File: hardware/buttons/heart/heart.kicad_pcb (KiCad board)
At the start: 2 copper layers, 24.5 x 26.3 mm, 10 parts, among them J1 Conn_01x03, J2 Conn_01x03

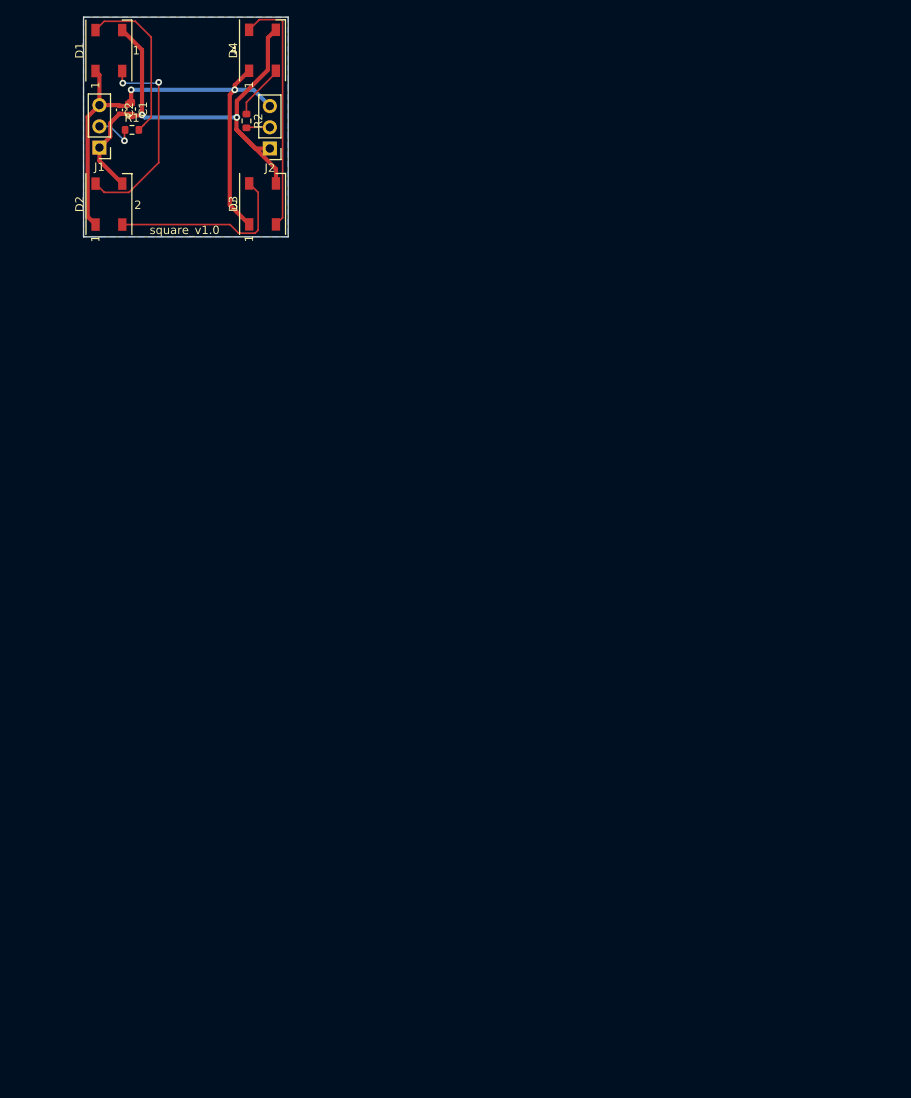
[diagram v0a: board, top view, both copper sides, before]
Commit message: Add heart button
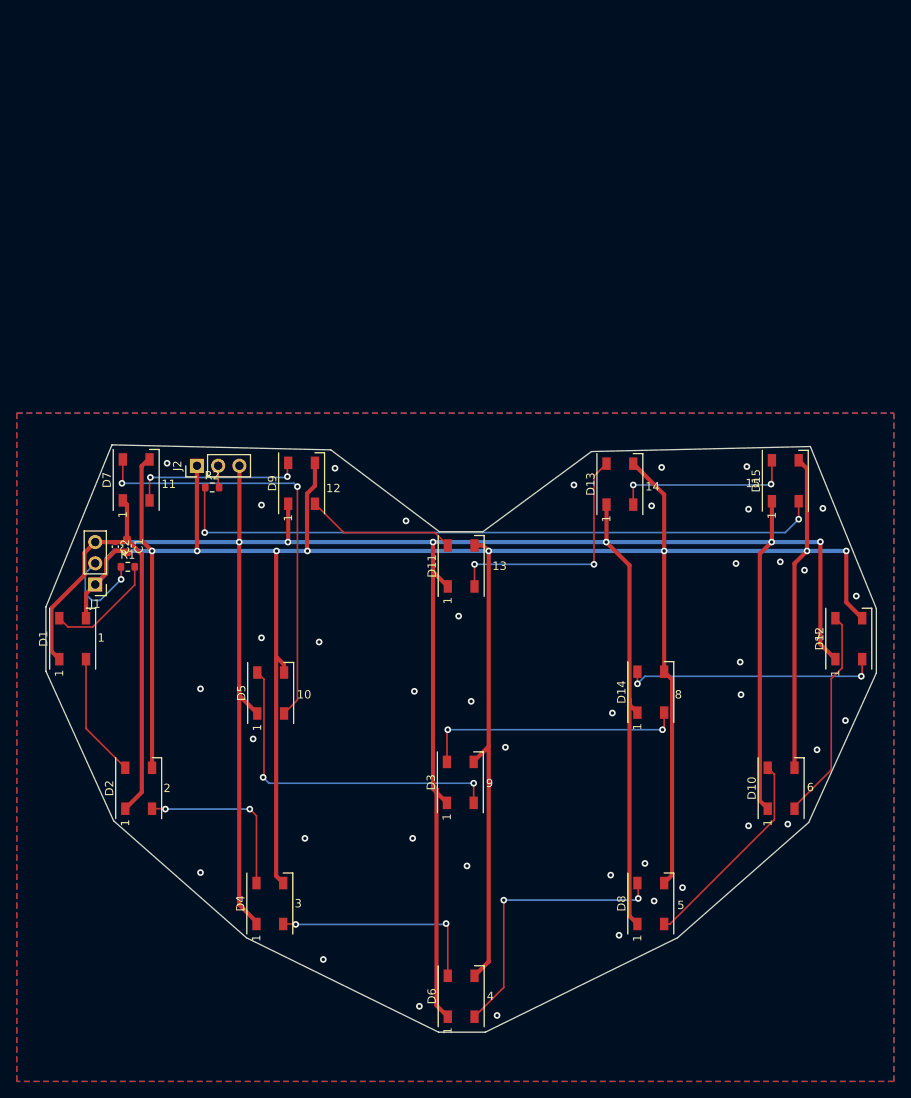
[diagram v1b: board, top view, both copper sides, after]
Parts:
- added D10: WS2812B, LED_SMD:LED_WS2812B_PLCC4_5.0x5.0mm_P3.2mm, F.Cu at (121.5, 124.9)
- added D11: WS2812B, LED_SMD:LED_WS2812B_PLCC4_5.0x5.0mm_P3.2mm, F.Cu at (83.2, 98.3)
- added D12: WS2812B, LED_SMD:LED_WS2812B_PLCC4_5.0x5.0mm_P3.2mm, F.Cu at (129.6, 107.0)
- added D13: WS2812B, LED_SMD:LED_WS2812B_PLCC4_5.0x5.0mm_P3.2mm, F.Cu at (102.2, 88.5)
- added D14: WS2812B, LED_SMD:LED_WS2812B_PLCC4_5.0x5.0mm_P3.2mm, F.Cu at (105.9, 113.4)
- added D15: WS2812B, LED_SMD:LED_WS2812B_PLCC4_5.0x5.0mm_P3.2mm, F.Cu at (122.0, 88.1)
- added D3: WS2812B, LED_SMD:LED_WS2812B_PLCC4_5.0x5.0mm_P3.2mm, F.Cu at (83.1, 124.2)
- added D5: WS2812B, LED_SMD:LED_WS2812B_PLCC4_5.0x5.0mm_P3.2mm, F.Cu at (60.4, 113.5)
- added D7: WS2812B, LED_SMD:LED_WS2812B_PLCC4_5.0x5.0mm_P3.2mm, F.Cu at (44.3, 88.0)
- added D8: WS2812B, LED_SMD:LED_WS2812B_PLCC4_5.0x5.0mm_P3.2mm, F.Cu at (105.9, 138.7)
- added D9: WS2812B, LED_SMD:LED_WS2812B_PLCC4_5.0x5.0mm_P3.2mm, F.Cu at (64.1, 88.4)
- moved D6 115.7 mm to (83.2, 149.8)
- moved D4 83.7 mm to (60.3, 138.7)
- moved D1 70.5 mm to (36.7, 107.0)
- moved D2 70.0 mm to (44.6, 124.9)
- moved C1 52.3 mm to (43.2, 95.9)
- moved R1 52.3 mm to (43.3, 98.4)
- moved C2 52.3 mm to (41.8, 96.0)
- moved J1 52.3 mm to (39.4, 100.5)
- moved R2 44.1 mm to (53.4, 88.9), turned to 0 degrees
- moved J2 39.0 mm to (51.6, 86.3), turned to 90 degrees
- renumbered D3 to D4, D4 to D6
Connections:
- D6 pad 2: Net-(D4-Pad2) (its old number) -> Net-(D6-Pad2)
- R2 pad 1: Net-(D4-Pad2) (its old number) -> Net-(D15-Pad2)
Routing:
- net VCC: track 63.3 -> 379.7 mm, vias 2 -> 6
- net GND: track 63.1 -> 360.4 mm, vias 2 -> 49
- net Net-(D15-Pad2): track 0.00 -> 79.3 mm, vias 0 -> 2
- net Net-(D5-Pad2): track 0.00 -> 51.9 mm, vias 0 -> 2
- net Net-(D3-Pad2): track 0.00 -> 40.8 mm, vias 0 -> 2
- net Net-(D6-Pad2): track 0.00 -> 33.5 mm, vias 0 -> 2
- net Net-(D14-Pad2): track 0.00 -> 31.7 mm, vias 0 -> 2
- net Net-(D12-Pad2): track 0.00 -> 30.7 mm, vias 0 -> 2
- net Net-(D11-Pad2): track 0.00 -> 29.6 mm, vias 0 -> 2
- net Net-(D10-Pad2): track 0.00 -> 25.5 mm
- net Net-(D10-Pad4): track 0.00 -> 24.9 mm
- net Net-(D13-Pad2): track 0.00 -> 21.8 mm, vias 0 -> 2
- net Net-(D7-Pad2): track 0.00 -> 20.9 mm, vias 0 -> 2
- net Net-(D11-Pad4): track 0.00 -> 18.0 mm
- net Net-(D1-Pad2): track 24.9 -> 14.9 mm, vias 2 -> 0
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- added copper zone on F.Cu, net GND
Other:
- board size 24.5 x 26.3 mm -> 99.4 x 70.3 mm
- board text added: "10"
- board text added: "11"
- board text added: "12"
- board text added: "13"
- board text added: "14"
- board text added: "15"
- board text added: "5"
- board text added: "6"
- board text added: "7"
- board text added: "8"
- board text added: "9"
- board text added: "heart_v1.0"
- board text removed: "square_v1.0"

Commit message: Add mounting holes
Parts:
- added H1: MountingHole, MountingHole:MountingHole_3.2mm_M3, F.Cu at (114.6, 103.7)
- added H2: MountingHole, MountingHole:MountingHole_3.2mm_M3, F.Cu at (68.0, 133.7)
- added H3: MountingHole, MountingHole:MountingHole_3.2mm_M3, F.Cu at (50.6, 103.7)
- added H4: MountingHole, MountingHole:MountingHole_3.2mm_M3, F.Cu at (98.9, 133.7)
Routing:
- net GND: vias 49 -> 48
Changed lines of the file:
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@@
     )
+  )
+  (footprint "MountingHole:MountingHole_3.2mm_M3" (layer "F.Cu")
+    (at 114.6 103.7)
+    (descr "Mounting Hole 3.2mm, no annular, M3")
+    (tags "mounting hole 3.2mm no annular m3")
+    (property "Sheetfile" "heart.kicad_sch")
+    (property "Sheetname" "")
+    (attr exclude_from_pos_files)
+    (fp_text reference "H1" (at 0 -4.2) (layer "F.SilkS")
+      (effects (font (size 1 1) (thickness 0.15)))
+    )
+    (fp_text value "MountingHole" (at 0 4.2) (layer "F.Fab")
+      (effects (font (size 1 1) (thickness 0.15)))
+    )
+    (fp_text user "${REFERENCE}" (at 0 0) (layer "F.Fab")
+      (effects (font (size 1 1) (thickness 0.15)))
+    )
+    (fp_circle (center 0 0) (end 3.2 0) (layer "Cmts.User") (width 0.15) (fill none))
+    (fp_circle (center 0 0) (end 3.45 0) (layer "F.CrtYd") (width 0.05) (fill none))
+    (pad "" np_thru_hole circle (at 0 0) (size 3.2 3.2) (drill 3.2) (layers *.Cu *.Mask))
+  )
+  (footprint "MountingHole:MountingHole_3.2mm_M3" (layer "F.Cu")
+    (at 50.576851 103.7)
+    (descr "Mounting Hole 3.2mm, no annular, M3")
+    (tags "mounting hole 3.2mm no annular m3")
+    (property "Sheetfile" "heart.kicad_sch")
+    (property "Sheetname" "")
+    (attr exclude_from_pos_files)
+    (fp_text reference "H3" (at 0 -4.2) (layer "F.SilkS")
+      (effects (font (size 1 1) (thickness 0.15)))
+    )
+    (fp_text value "MountingHole" (at 0 4.2) (layer "F.Fab")
+      (effects (font (size 1 1) (thickness 0.15)))
+    )
+    (fp_text user "${REFERENCE}" (at 0 0) (layer "F.Fab")
+      (effects (font (size 1 1) (thickness 0.15)))
+    )
+    (fp_circle (center 0 0) (end 3.2 0) (layer "Cmts.User") (width 0.15) (fill none))
+    (fp_circle (center 0 0) (end 3.45 0) (layer "F.CrtYd") (width 0.05) (fill none))
+    (pad "" np_thru_hole circle (at 0 0) (size 3.2 3.2) (drill 3.2) (layers *.Cu *.Mask))
   )
   (footprint "LED_SMD:LED_WS2812B_PLCC4_5.0x5.0mm_P3.2mm" (layer "F.Cu")
@@
     )
   )
+  (footprint "MountingHole:MountingHole_3.2mm_M3" (layer "F.Cu")
+    (at 68 133.7)
+    (descr "Mounting Hole 3.2mm, no annular, M3")
+    (tags "mounting hole 3.2mm no annular m3")
+    (property "Sheetfile" "heart.kicad_sch")
+    (property "Sheetname" "")
+    (attr exclude_from_pos_files)
+    (fp_text reference "H2" (at 0 -4.2) (layer "F.SilkS")
+      (effects (font (size 1 1) (thickness 0.15)))
+    )
+    (fp_text value "MountingHole" (at 0 4.2) (layer "F.Fab")
+      (effects (font (size 1 1) (thickness 0.15)))
+    )
+    (fp_text user "${REFERENCE}" (at 0 0) (layer "F.Fab")
+      (effects (font (size 1 1) (thickness 0.15)))
+    )
+    (fp_circle (center 0 0) (end 3.2 0) (layer "Cmts.User") (width 0.15) (fill none))
+    (fp_circle (center 0 0) (end 3.45 0) (layer "F.CrtYd") (width 0.05) (fill none))
+    (pad "" np_thru_hole circle (at 0 0) (size 3.2 3.2) (drill 3.2) (layers *.Cu *.Mask))
+  )
   (footprint "Capacitor_SMD:C_0402_1005Metric" (layer "F.Cu")
     (at 41.8 96 -90)
@@
       (rotate (xyz 0 0 0))
     )
+  )
+  (footprint "MountingHole:MountingHole_3.2mm_M3" (layer "F.Cu")
+    (at 98.9 133.7)
+    (descr "Mounting Hole 3.2mm, no annular, M3")
+    (tags "mounting hole 3.2mm no annular m3")
+    (property "Sheetfile" "heart.kicad_sch")
+    (property "Sheetname" "")
+    (attr exclude_from_pos_files)
+    (fp_text reference "H4" (at 0 -4.2) (layer "F.SilkS")
+      (effects (font (size 1 1) (thickness 0.15)))
+    )
+    (fp_text value "MountingHole" (at 0 4.2) (layer "F.Fab")
+      (effects (font (size 1 1) (thickness 0.15)))
+    )
+    (fp_text user "${REFERENCE}" (at 0 0) (layer "F.Fab")
+      (effects (font (size 1 1) (thickness 0.15)))
+    )
+    (fp_circle (center 0 0) (end 3.2 0) (layer "Cmts.User") (width 0.15) (fill none))
+    (fp_circle (center 0 0) (end 3.45 0) (layer "F.CrtYd") (width 0.05) (fill none))
+    (pad "" np_thru_hole circle (at 0 0) (size 3.2 3.2) (drill 3.2) (layers *.Cu *.Mask))
   )
   (footprint "Connector_PinHeader_2.54mm:PinHeader_1x03_P2.54mm_Vertical" (layer "F.Cu")
@@
   (via (at 116.6 109.8) (size 0.8) (drill 0.4) (layers "F.Cu" "B.Cu") (free) (net 2))
   (via (at 66.7 145.4) (size 0.8) (drill 0.4) (layers "F.Cu" "B.Cu") (free) (net 2))
-  (via (at 101.1 135.3) (size 0.8) (drill 0.4) (layers "F.Cu" "B.Cu") (free) (net 2))
   (segment (start 46.2 96.5) (end 48 96.5) (width 0.5) (layer "B.Cu") (net 2))
   (segment (start 107.5 96.5) (end 124.6 96.5) (width 0.5) (layer "B.Cu") (net 2))
